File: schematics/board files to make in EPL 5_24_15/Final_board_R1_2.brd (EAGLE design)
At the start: 99.1 x 74.9 mm, 50 parts, among them Q2 16MHz, U1 ATMEGA328P-PU, U2 CD4066BE

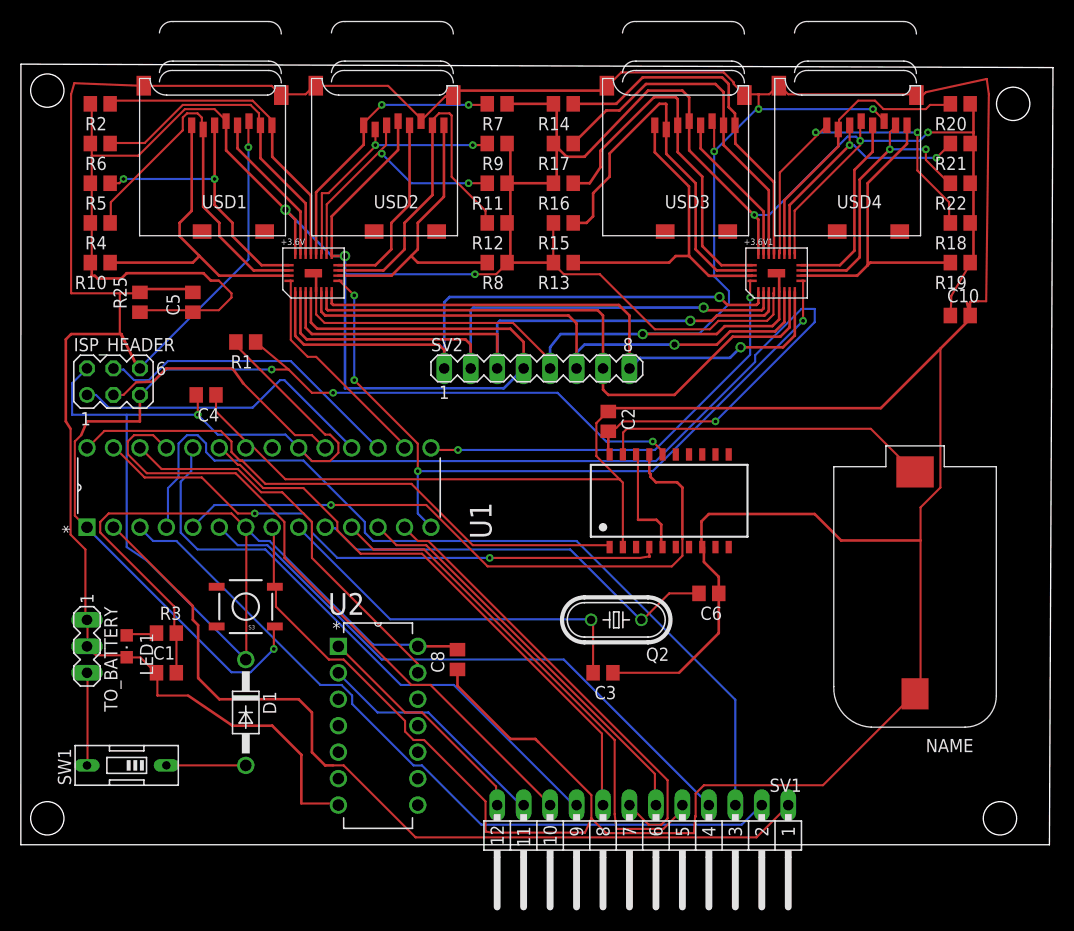
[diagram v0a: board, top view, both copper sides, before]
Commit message: Uploaded new layout for routing
Had to rework board layout to accommodate current LPKF router
functionality(2 tooling slots out of order, limited to max 10 instead of
12 tools for job).  I'm including gerber files from CAM processing.  The
top, bottom, outline .gbx files are needed, as well as the .xln drill
file, to import into the routing program.
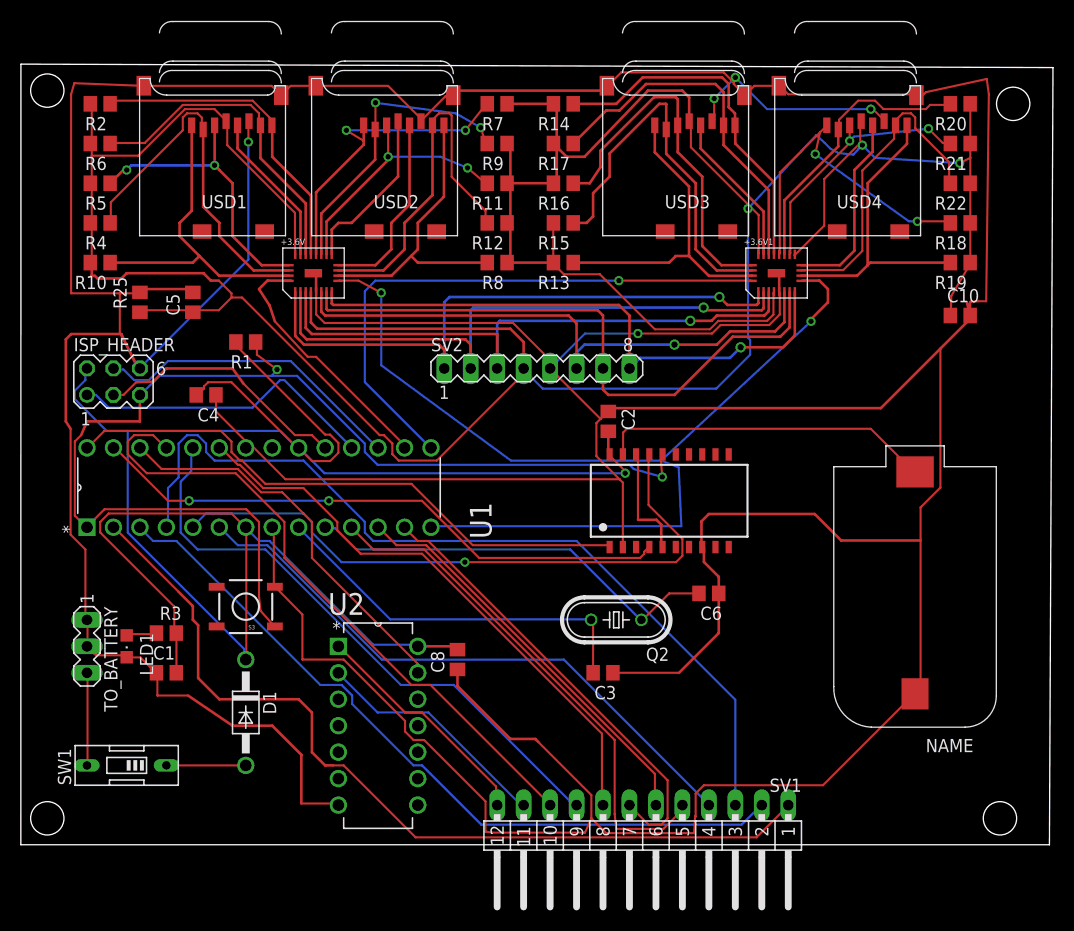
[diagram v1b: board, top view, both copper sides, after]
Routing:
- net VCC: track 233.2 -> 194.0 mm, vias 2 -> 1
- net S: track 74.5 -> 99.1 mm, vias 4 -> 2
- net VDDH: track 331.6 -> 354.4 mm, vias 6 -> 3
- net GND: track 657.6 -> 638.5 mm
- net /OE1: track 41.8 -> 55.3 mm, vias 2 -> 1
- net N$5: track 104.4 -> 108.9 mm, vias 4 -> 2
- net N$35: track 27.2 -> 31.0 mm
- net N$32: track 25.3 -> 28.9 mm
- net /OE2: track 21.3 -> 24.8 mm
- net N$47: track 34.3 -> 31.5 mm
- net N$45: track 28.0 -> 30.6 mm, vias 2 -> 0
- net N$25: track 63.0 -> 61.4 mm
- net N$36: track 26.3 -> 25.2 mm
- net N$4: track 57.5 -> 56.4 mm
- net N$30: track 28.1 -> 28.7 mm
